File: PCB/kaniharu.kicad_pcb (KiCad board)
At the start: 4 copper layers, 75.1 x 50.4 mm, 97 parts, among them J2 USB_C_Receptacle_USB2.0_14P, J3 Conn_02x03_Odd_Even, J4 Conn_02x03_Odd_Even, J5 Conn_02x03_Odd_Even, J6 RJ45_Pulse_JXD6-0001NL, U1 STM32H723VGTx, U2 ISO1044BD, U3 ISO1044BD, U4 AZ1117-3.3, U6 DP83848C, U7 ISO1044BD, Y1 CSTNE16M0V53C000R0, Y2 50M

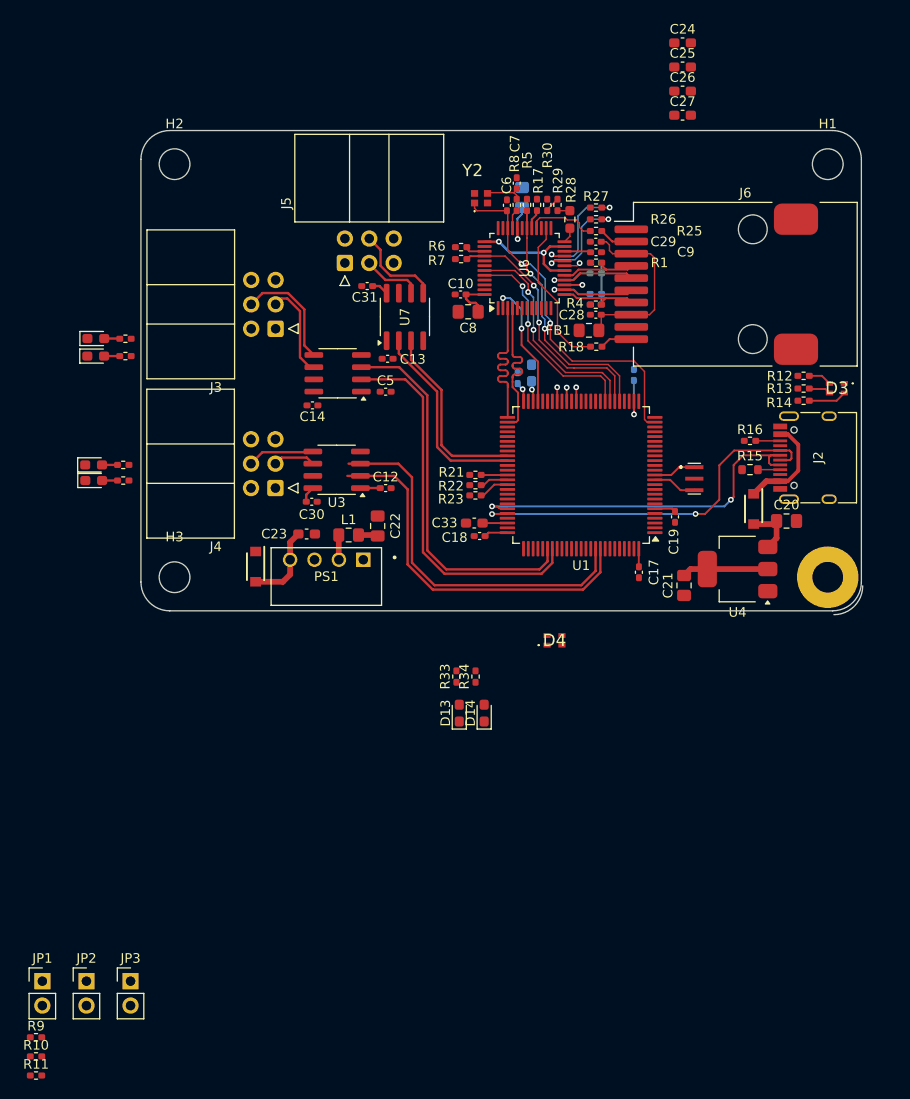
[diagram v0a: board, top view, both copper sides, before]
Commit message: 電源以外配線おわり
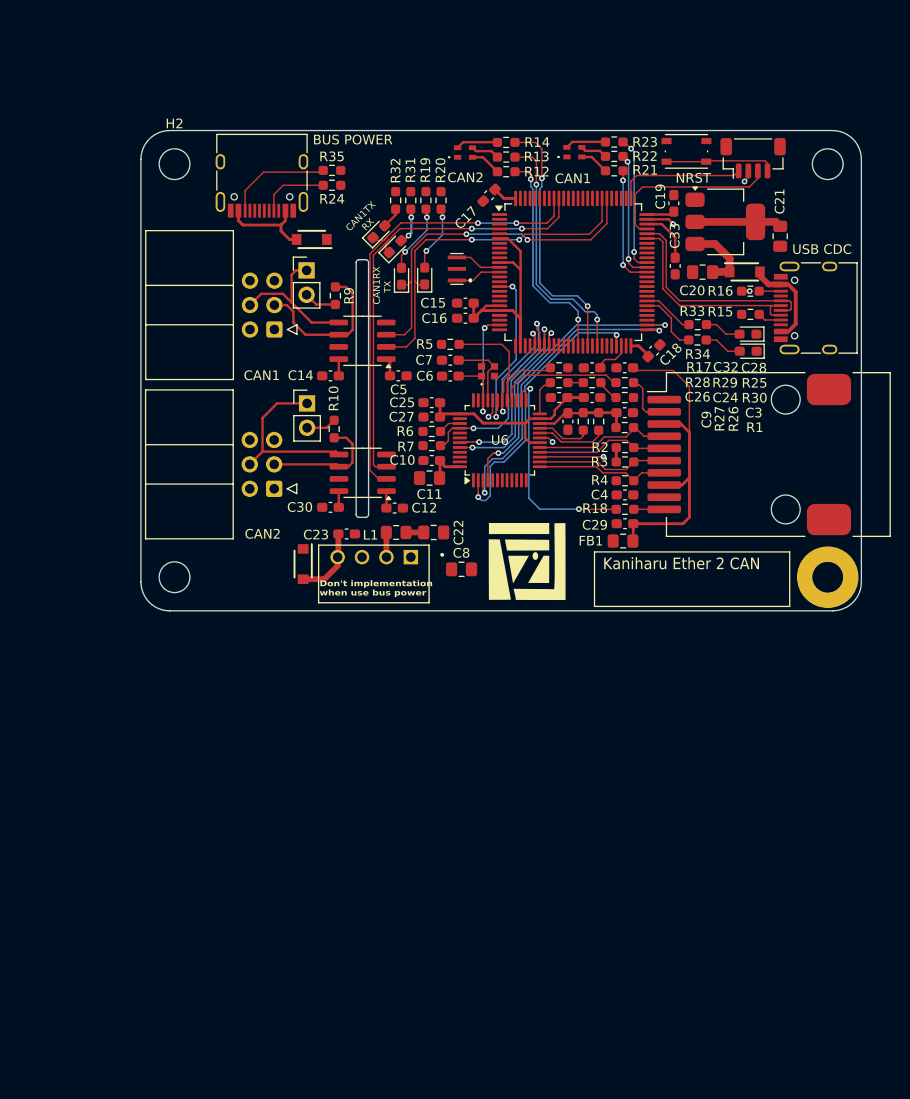
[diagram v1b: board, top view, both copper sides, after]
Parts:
- removed C13, C31: 0.1u, Capacitor_SMD:C_0402_1005Metric_Pad0.74x0.62mm_HandSolder
- removed D13, D14: LED, LED_SMD:LED_0603_1608Metric_Pad1.05x0.95mm_HandSolder
- removed J5: Conn_02x03_Odd_Even, Connector_IDC:IDC-Header_2x03_P2.54mm_Horizontal
- removed JP3: Jumper_2_Open, Connector_PinHeader_2.54mm:PinHeader_1x02_P2.54mm_Vertical
- removed R11, R8: R, Resistor_SMD:R_0402_1005Metric_Pad0.72x0.64mm_HandSolder
- removed U7: ISO1044BD, Package_SO:SOIC-8_3.9x4.9mm_P1.27mm
- added D7: D, 0_syslib:SODFL3618X110N, F.Cu at (117.8, 91.3)
- added D8: LED, LED_SMD:LED_0603_1608Metric_Pad1.05x0.95mm_HandSolder, F.Cu at (163.2, 101.2)
- added D9: LED, LED_SMD:LED_0603_1608Metric_Pad1.05x0.95mm_HandSolder, F.Cu at (163.2, 103.0)
- added G***: LOGO, 0_mylib:robopro_logo_small, F.Cu at (140.2, 124.9)
- added J1: Conn_01x04, Connector_JST:JST_SH_BM04B-SRSS-TB_1x04-1MP_P1.00mm_Vertical, F.Cu at (163.7, 82.9)
- added J7: USB_C_Receptacle_USB2.0_14P, Connector_USB:USB_C_Receptacle_HRO_TYPE-C-31-M-12, F.Cu at (112.6, 84.3)
- added R24: 4.7k, Resistor_SMD:R_0603_1608Metric_Pad0.98x0.95mm_HandSolder, F.Cu at (119.9, 85.7)
- added R35: 4.7k, Resistor_SMD:R_0603_1608Metric_Pad0.98x0.95mm_HandSolder, F.Cu at (119.9, 84.2)
- added SW1: SW_Push, Button_Switch_SMD:SW_Push_1P1T_NO_Vertical_Wuerth_434133025816, F.Cu at (156.8, 82.2)
- C10, C12, C14, C17, C18, C19, C28, C29, C30, C5, C6, C7, C9: footprint Capacitor_SMD:C_0402_1005Metric_Pad0.74x0.62mm_HandSolder -> Capacitor_SMD:C_0603_1608Metric_Pad1.08x0.95mm_HandSolder
- C11, C32: moved to F.Cu
- C15, C16, C3, C4: footprint Capacitor_SMD:C_0402_1005Metric_Pad0.74x0.62mm_HandSolder -> Capacitor_SMD:C_0603_1608Metric_Pad1.08x0.95mm_HandSolder; moved to F.Cu
- R1, R10, R12, R13, R14, R16, R17, R18, R19, R20, R21, R22, R23, R25, R26, R27, R29, R30, R31, R32, R33, R34, R4, R5, R6, R7, R9: footprint Resistor_SMD:R_0402_1005Metric_Pad0.72x0.64mm_HandSolder -> Resistor_SMD:R_0603_1608Metric_Pad0.98x0.95mm_HandSolder
- R15: footprint Resistor_SMD:R_0603_1608Metric -> Resistor_SMD:R_0603_1608Metric_Pad0.98x0.95mm_HandSolder
- R2, R3: footprint Resistor_SMD:R_0402_1005Metric_Pad0.72x0.64mm_HandSolder -> Resistor_SMD:R_0603_1608Metric_Pad0.98x0.95mm_HandSolder; moved to F.Cu
- moved R9 83.3 mm to (120.2, 97.2), turned to 90 degrees
- moved JP1 78.9 mm to (117.2, 94.6)
- moved R10 72.3 mm to (120.1, 111.1), turned to -90 degrees
- moved JP2 64.4 mm to (117.3, 108.4)
- moved D4 50.9 mm to (145.1, 82.3)
- moved D3 45.8 mm to (133.7, 82.3), turned to 180 degrees
- moved R33 44.4 mm to (158.0, 100.2), turned to 0 degrees
- moved C25 43.6 mm to (130.3, 108.3), turned to 180 degrees
- moved C17 42.2 mm to (136.2, 86.7), turned to -135 degrees
- moved R34 42.0 mm to (157.9, 101.8), turned to 0 degrees
- moved R31 41.8 mm to (128.1, 87.3), turned to -90 degrees
- moved R14 41.0 mm to (138.0, 81.2), turned to 180 degrees
- moved C27 40.9 mm to (130.3, 109.8), turned to 180 degrees
- moved D11 39.7 mm to (126.5, 92.1), turned to 45 degrees
- moved R32 39.5 mm to (126.5, 87.3), turned to -90 degrees
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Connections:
- C14 pad 2: GND -> GNDPWR
- C30 pad 2: GND -> GNDPWR
- C7 pad 1: Net-(C7-Pad1) -> Net-(U6-X2)
- D2 pad 1: Net-(D2-K) -> +5V
- D2 pad 2: +5V -> Net-(D2-A)
- J2 pad A4: Net-(D2-K) -> Net-(D2-A)
- J2 pad A9: Net-(D2-K) -> Net-(D2-A)
- J2 pad B4: Net-(D2-K) -> Net-(D2-A)
- J2 pad B9: Net-(D2-K) -> Net-(D2-A)
- R33 pad 1: +3.3V -> Net-(U1-PD10)
- R34 pad 1: +3.3V -> Net-(U1-PD9)
- U1 pad 14: Net-(U1-NRST) -> NRST
- U1 pad 56: unconnected-(U1-PD9-Pad56) -> Net-(U1-PD9)
- U1 pad 57: unconnected-(U1-PD10-Pad57) -> Net-(U1-PD10)
- U1 pad 59: /CAN3/FDCAN3_RX -> /MCU/FDCAN3_RX
- U1 pad 60: /CAN3/FDCAN3_TX -> /MCU/FDCAN3_TX
- Y2 pad 3: Net-(C7-Pad1) -> Net-(U6-X2)
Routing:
- net /MCU/TIM1_CH2: track 1.43 -> 27.3 mm, vias 1 -> 2
- net /MCU/TIM1_CH3: track 1.46 -> 26.1 mm, vias 1 -> 2
- net +3.3V: track 41.0 -> 62.6 mm, vias 3 -> 1
- net /MCU/TIM1_CH1: track 1.46 -> 22.9 mm, vias 1 -> 2
- net /CAN3/FDCAN3_TX: track 20.6 -> 0.00 mm
- net /ETH/ETH_REF_CLK: track 37.2 -> 16.6 mm
- net /CAN3/FDCAN3_RX: track 19.5 -> 0.00 mm
- net SWDIO: track 0.00 -> 18.8 mm
- net /ETH/ETH_TXD0: track 16.0 -> 34.3 mm, vias 0 -> 2
- net /ETH/ETH_MDC: track 0.00 -> 17.7 mm, vias 0 -> 2
- net /MCU/USB_OTG_FS_DM: track 38.9 -> 21.7 mm, vias 2 -> 0
- net /MCU/USB_OTG_FS_DP: track 39.7 -> 22.7 mm, vias 2 -> 0
- net /ETH/ETH_TX_EN: track 13.7 -> 30.0 mm
- net /ETH/ETH_TXD1: track 16.2 -> 31.7 mm, vias 0 -> 2
- net Net-(J6-RCT): track 19.5 -> 34.3 mm
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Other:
- board size 75.1 x 50.4 mm -> 75 x 50 mm
- board text added: "BUS POWER"
- board text added: "CAN1"
- board text added: "CAN1RX TX"
- board text added: "CAN1TX RX"
- board text added: "CAN2"
- board text added: "Don't implementation when use bus power"
- board text added: "Kaniharu Ether 2 CAN"
- board text added: "NRST"
- board text added: "USB CDC"

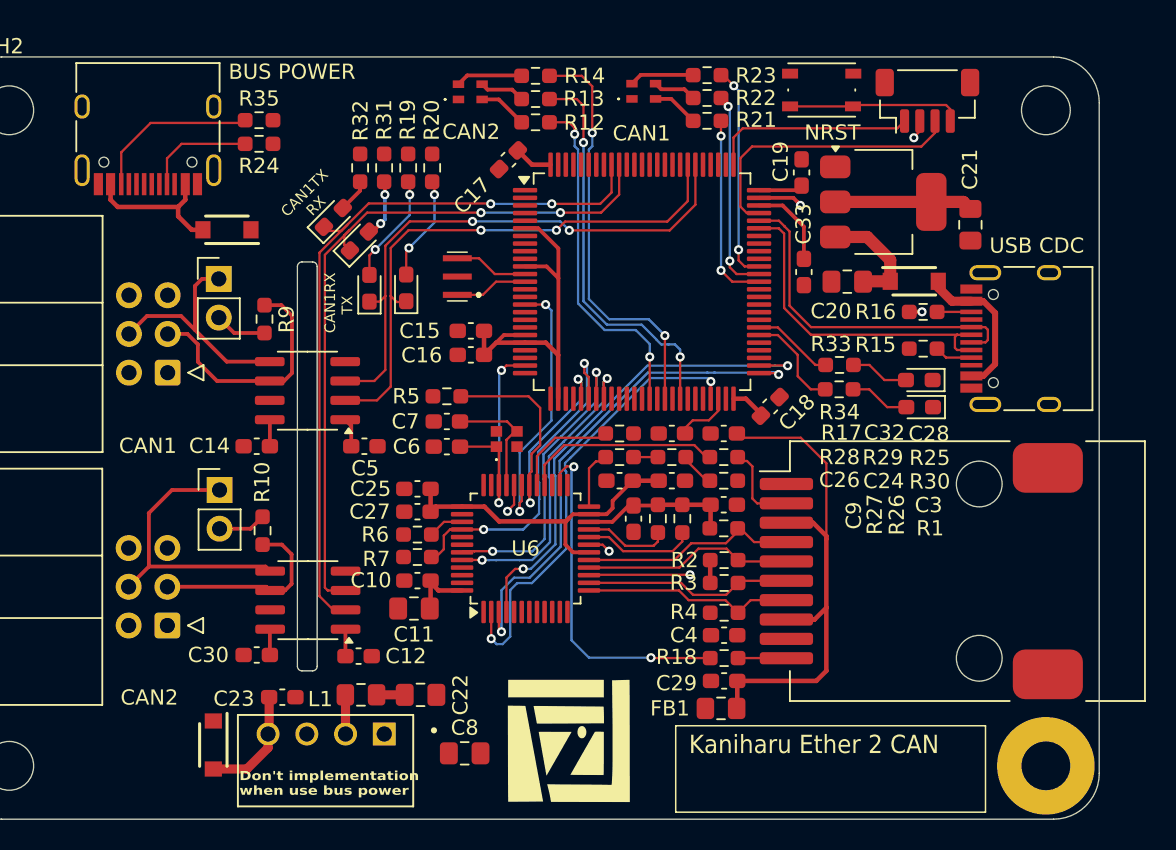
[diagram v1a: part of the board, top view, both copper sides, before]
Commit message: update
電源配線した
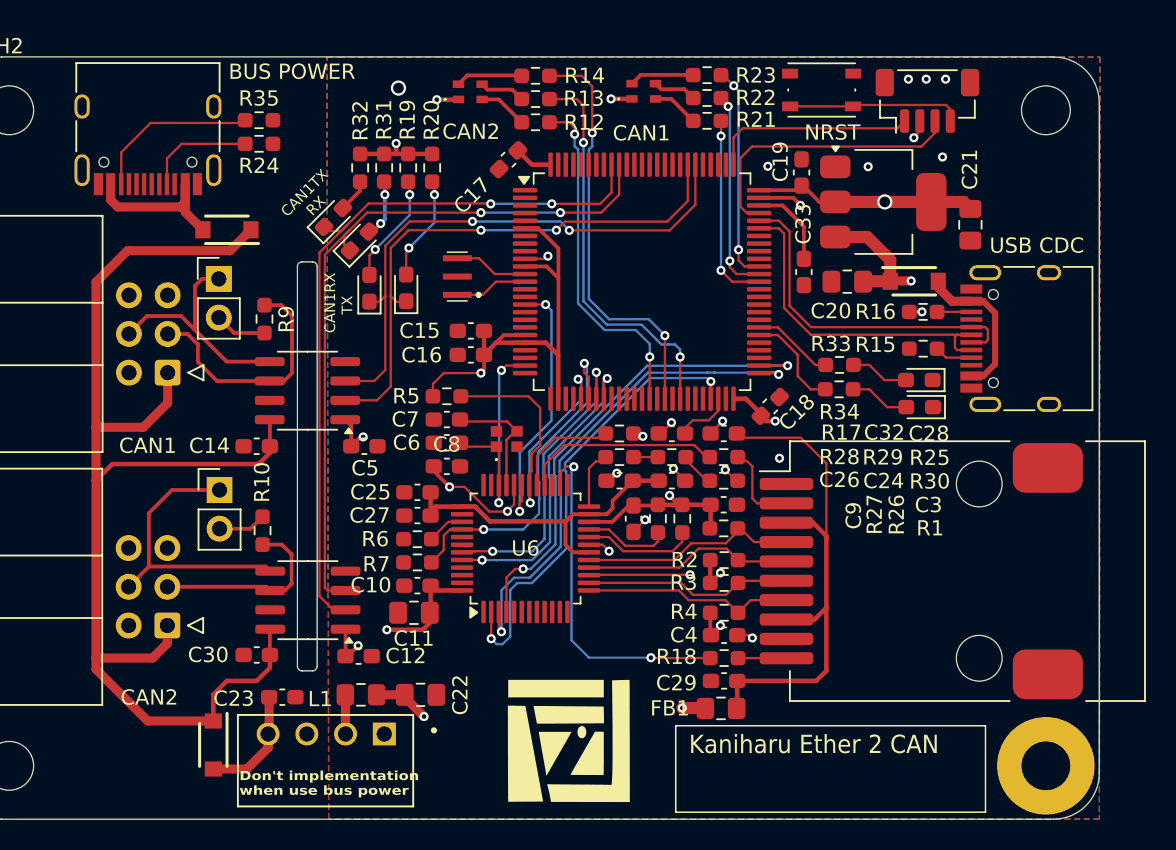
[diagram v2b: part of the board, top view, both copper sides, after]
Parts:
- C8: value 10u -> 0.1u; footprint Capacitor_SMD:C_0805_2012Metric_Pad1.18x1.45mm_HandSolder -> Capacitor_SMD:C_0603_1608Metric_Pad1.08x0.95mm_HandSolder
- moved C8 18.9 mm to (132.2, 106.9)
- moved R7 0.36 mm to (130.3, 113.2)
- moved C10 0.33 mm to (130.3, 114.7)
- moved R6 0.30 mm to (130.3, 111.6)
- moved C11 0.28 mm to (130.0, 116.5)
- moved C27 0.25 mm to (130.3, 110.1)
- moved C6 0.25 mm to (132.2, 105.3)
- moved C25 0.23 mm to (130.3, 108.6)
- moved C7 0.13 mm to (132.2, 103.8)
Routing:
- net +3.3V: track 62.6 -> 242.8 mm, vias 1 -> 17
- net +5VA: track 3.44 -> 82.7 mm
- net +5V: track 9.65 -> 83.1 mm, vias 0 -> 2
- net GND: track 13.2 -> 22.3 mm, vias 5 -> 20
- net Net-(D7-A): track 9.94 -> 10.9 mm
- added copper zone on B.Cu, net GND
- added copper zone on F.Cu, net GND
- added copper zone on In1.Cu, net GND

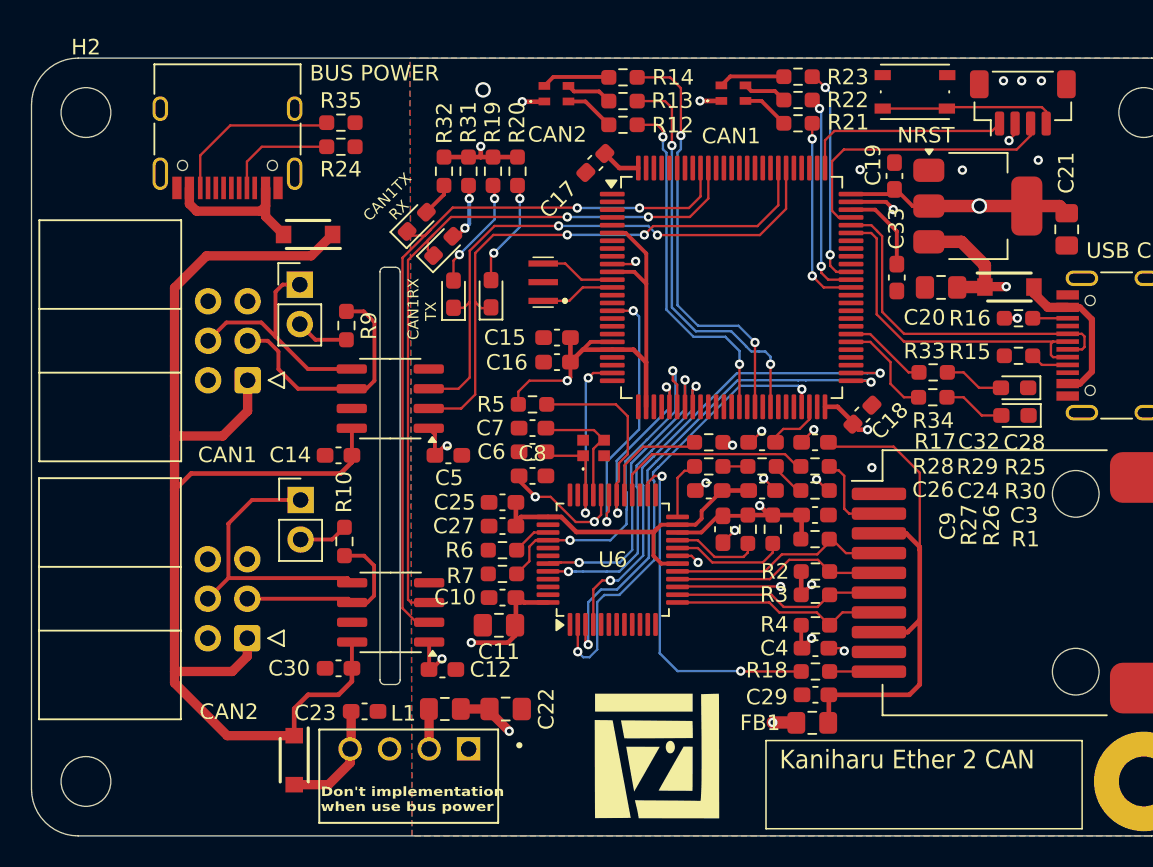
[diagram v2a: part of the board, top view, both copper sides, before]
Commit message: ベタを配置
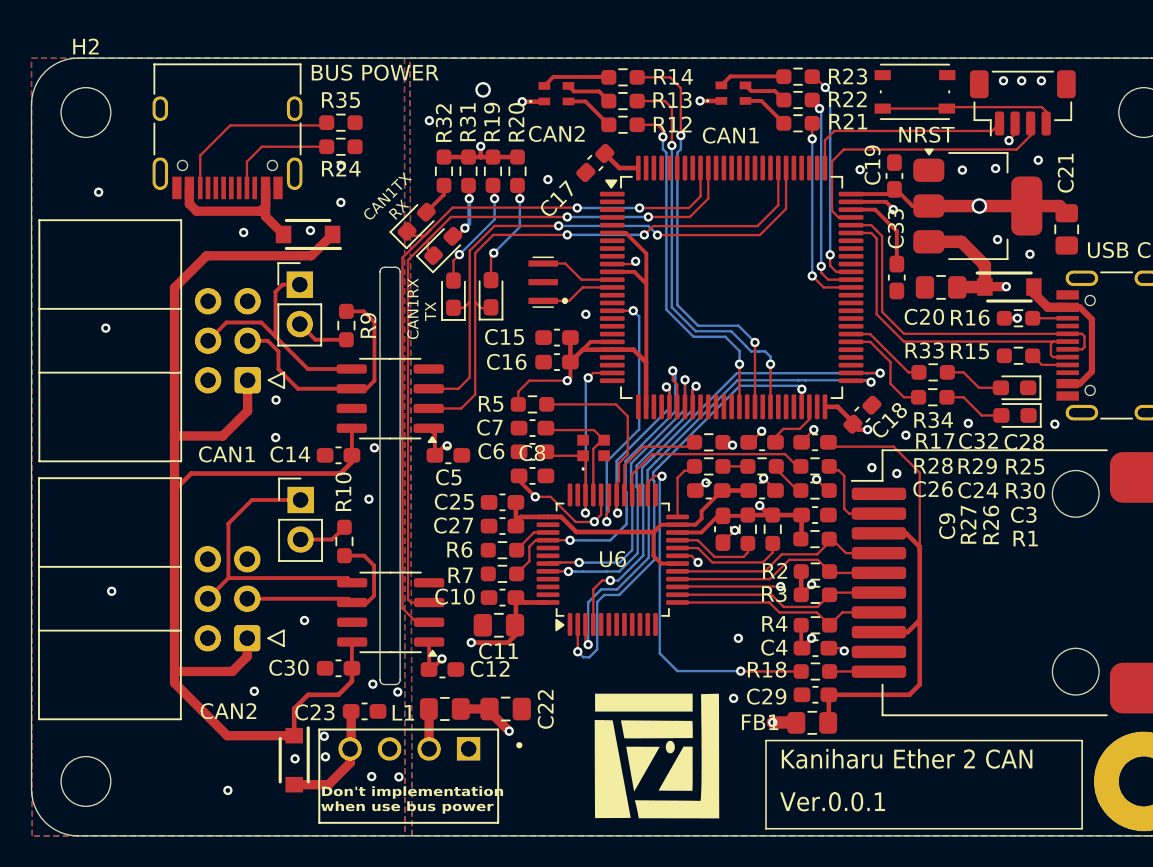
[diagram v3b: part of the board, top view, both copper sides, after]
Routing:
- net GNDPWR: vias 0 -> 21
- net GND: vias 20 -> 32
- added copper zone on B.Cu, net GNDPWR
- added copper zone on F.Cu, net GNDPWR
- added copper zone on In1.Cu, net GNDPWR
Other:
- board text added: "Ver.0.0.1"
